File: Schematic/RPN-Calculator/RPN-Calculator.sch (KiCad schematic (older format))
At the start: 33 parts

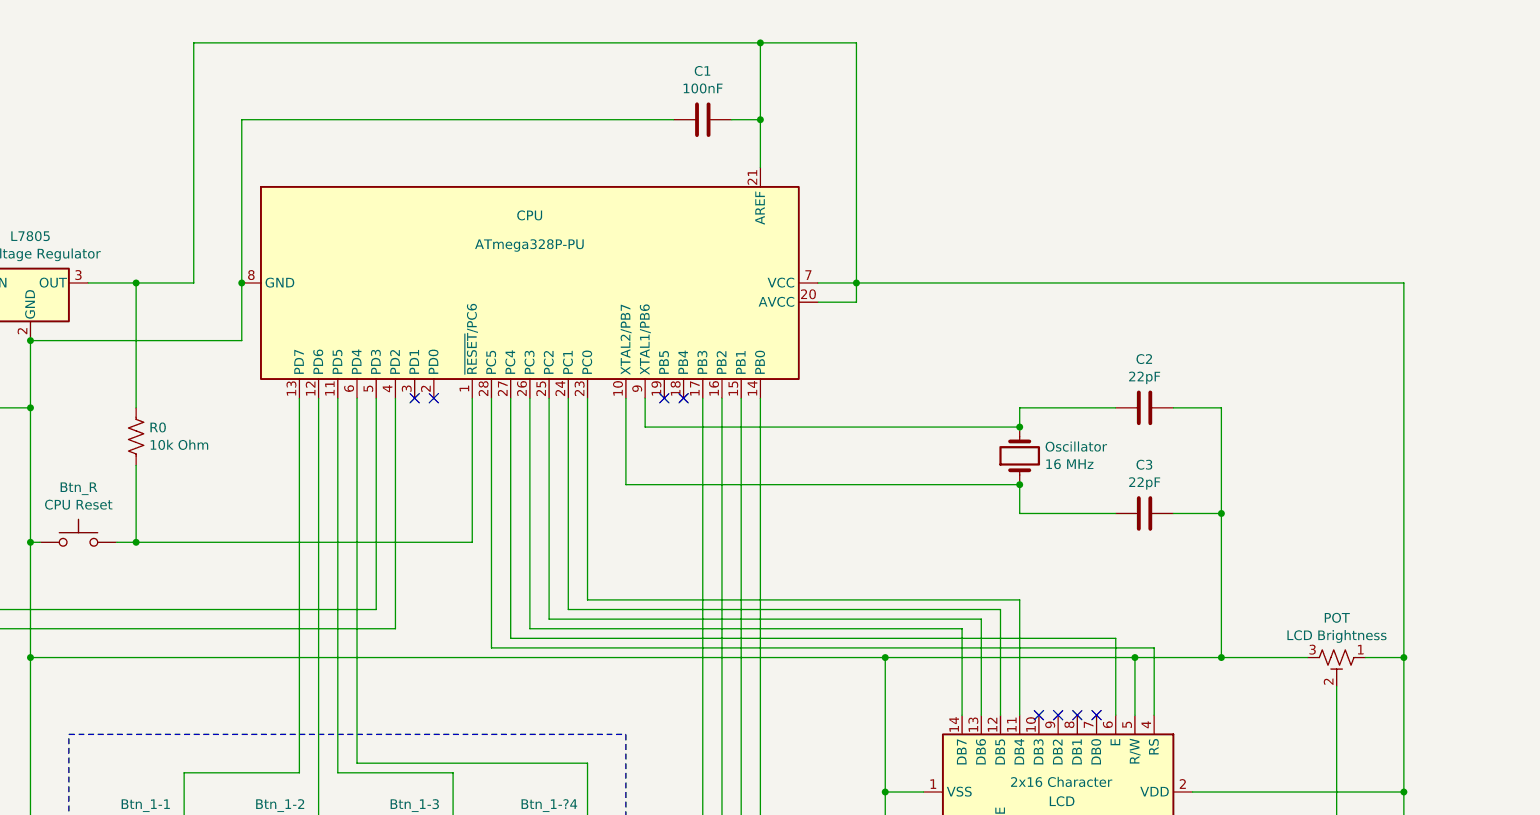
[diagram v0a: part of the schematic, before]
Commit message: Label Gnd and 5V wires
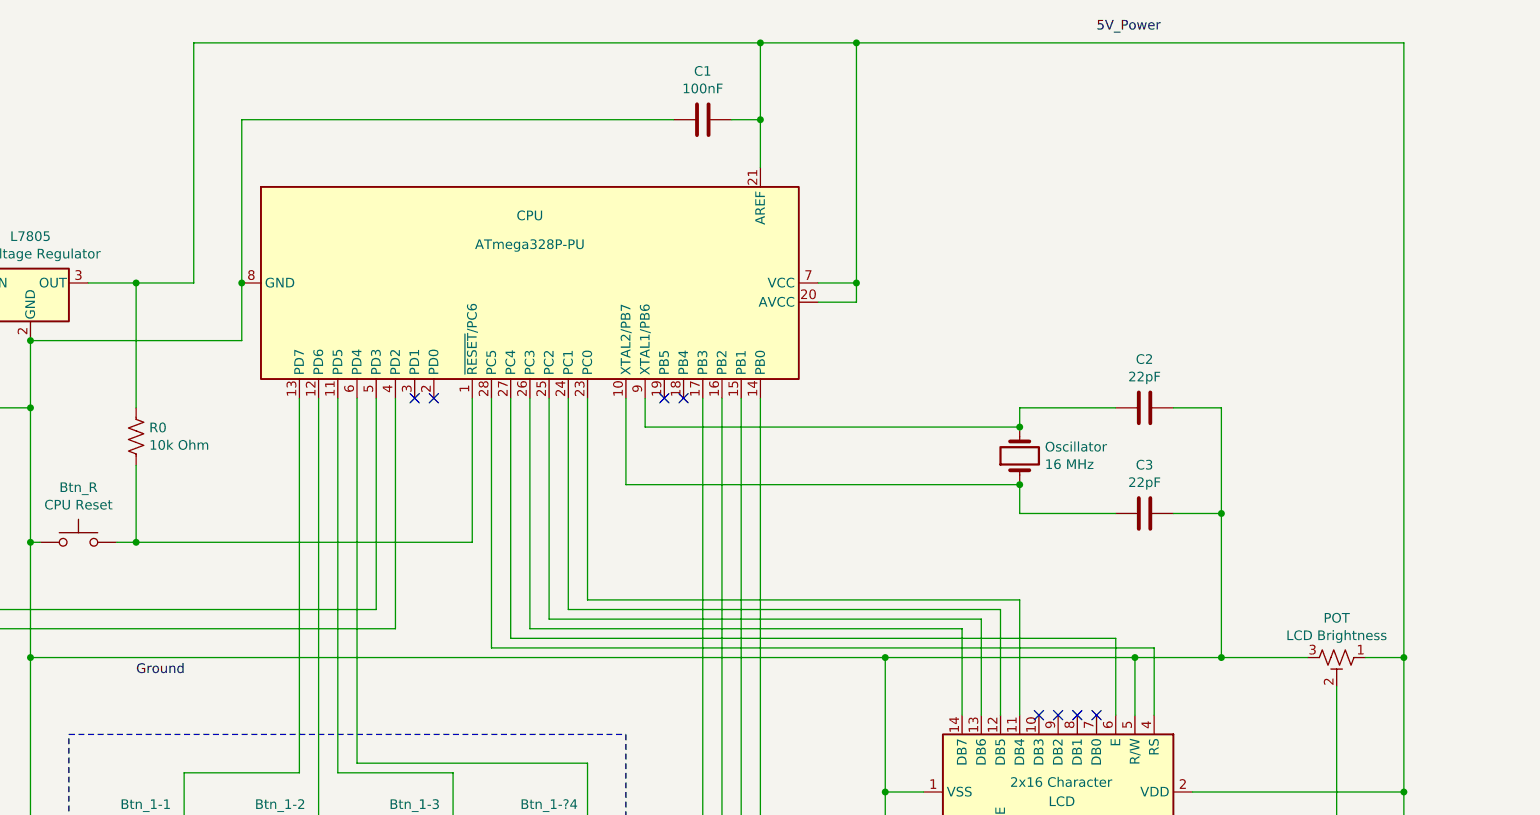
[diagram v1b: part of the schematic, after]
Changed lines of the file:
@@
 Wire Wire Line
 	8100 4900 9200 4900
-Wire Wire Line
-	6350 2250 9200 2250
 Connection ~ 4950 5250
 Connection ~ 4550 5400
@@
 Wire Wire Line
 	1500 2650 1500 2900
-Wire Wire Line
-	9200 2250 9200 4200
 Wire Wire Line
 	8250 4200 8700 4200
@@
 Wire Wire Line
 	6350 2350 6350 2250
+Wire Wire Line
+	6350 1000 9200 1000
+Wire Wire Line
+	9200 1000 9200 4200
+Connection ~ 6350 1000
+Text Label 7600 950  0    50   ~ 0
+5V_Power
+Text Label 2600 4300 0    50   ~ 0
+Ground
 $EndSCHEMATC
